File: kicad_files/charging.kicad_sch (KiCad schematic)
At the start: 22 parts, among them Q1 AO3400A, Q2 AO3400A, Q3 AO3401A, Q5 Q_PMOS, U2 BQ24172RGYR, U3 CYPD3177-24LQ

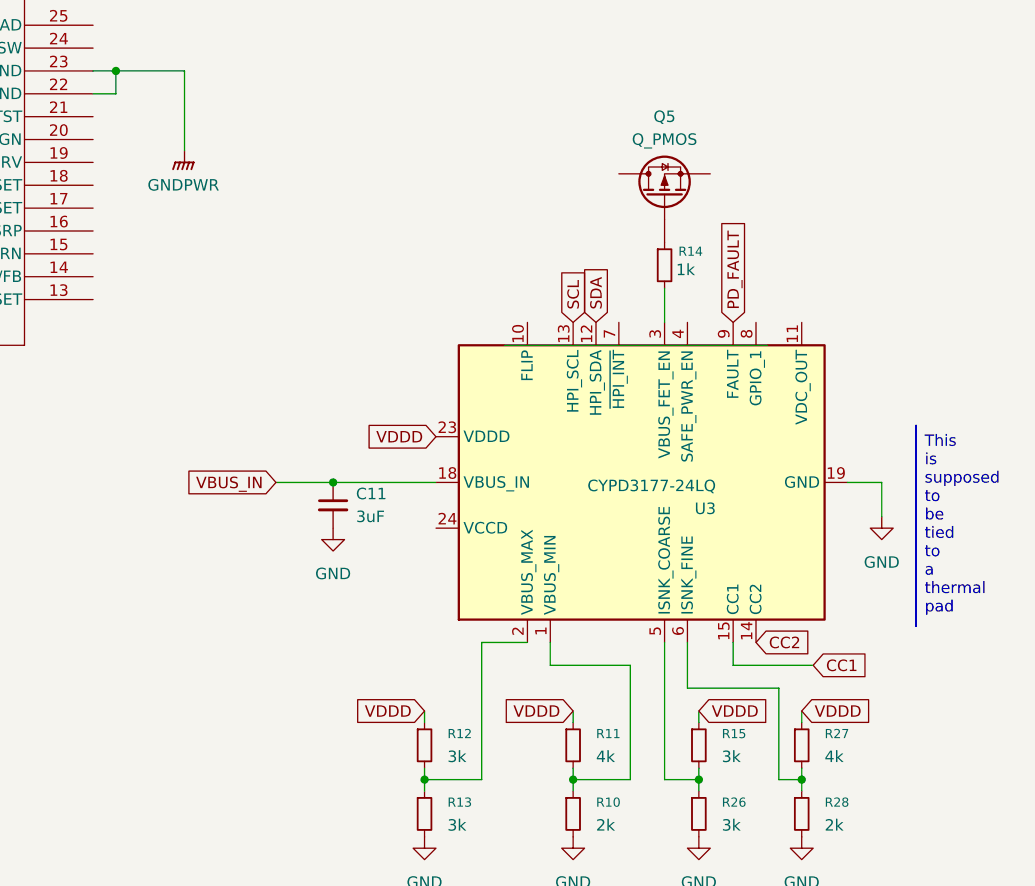
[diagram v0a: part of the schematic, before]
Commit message: fixing up some labels
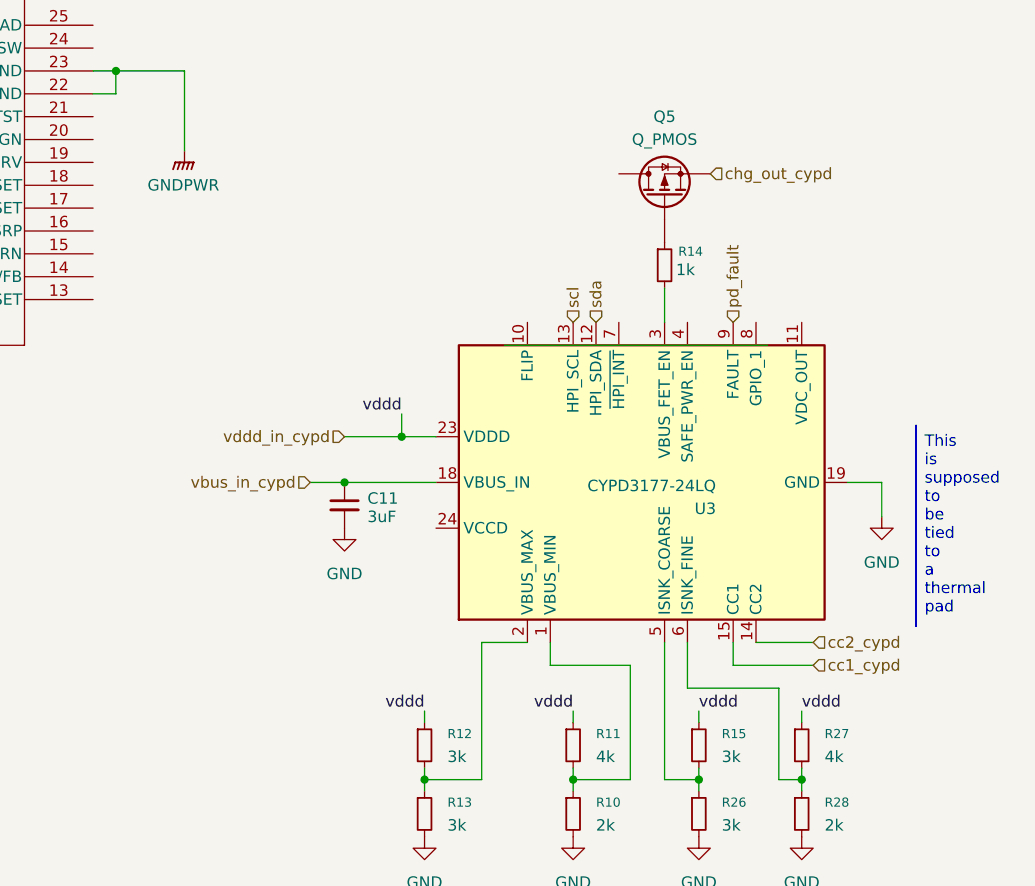
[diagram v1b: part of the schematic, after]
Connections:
- net chg_out_cypd: now reaches Q5.S
- net CC1 renamed cc1_cypd
- net CC2 renamed cc2_cypd
- net PD_FAULT renamed pd_fault
- net SCL renamed scl
- net SDA renamed sda
- net VBUS_IN renamed vbus_in_cypd
- net VDDD renamed vddd_in_cypd
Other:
- moved on the sheet: C11

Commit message: Fix grid alignment issues with charging hierarchical sheet
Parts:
- renumbered R12 to R10, R13 to R11, R11 to R12, R10 to R13, R26 to R20, R27 to R21, R28 to R26

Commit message: A little more progress on BQ24172 IC
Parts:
- added R27: 10m, symbol Device:R_Small
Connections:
- net GNDA: now also C10.1; no longer C10.2
- net Vsys: now also C10.2, C9.2, U2.5 (ACN), R27.2; no longer Q2.3 (D)
- net at C9.1: now also Q2.3 (D), U2.6 (ACP), R27.1; no longer U2.5 (ACN)
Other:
- moved on the sheet: C10, C9, Q1, Q2, Q3, R9

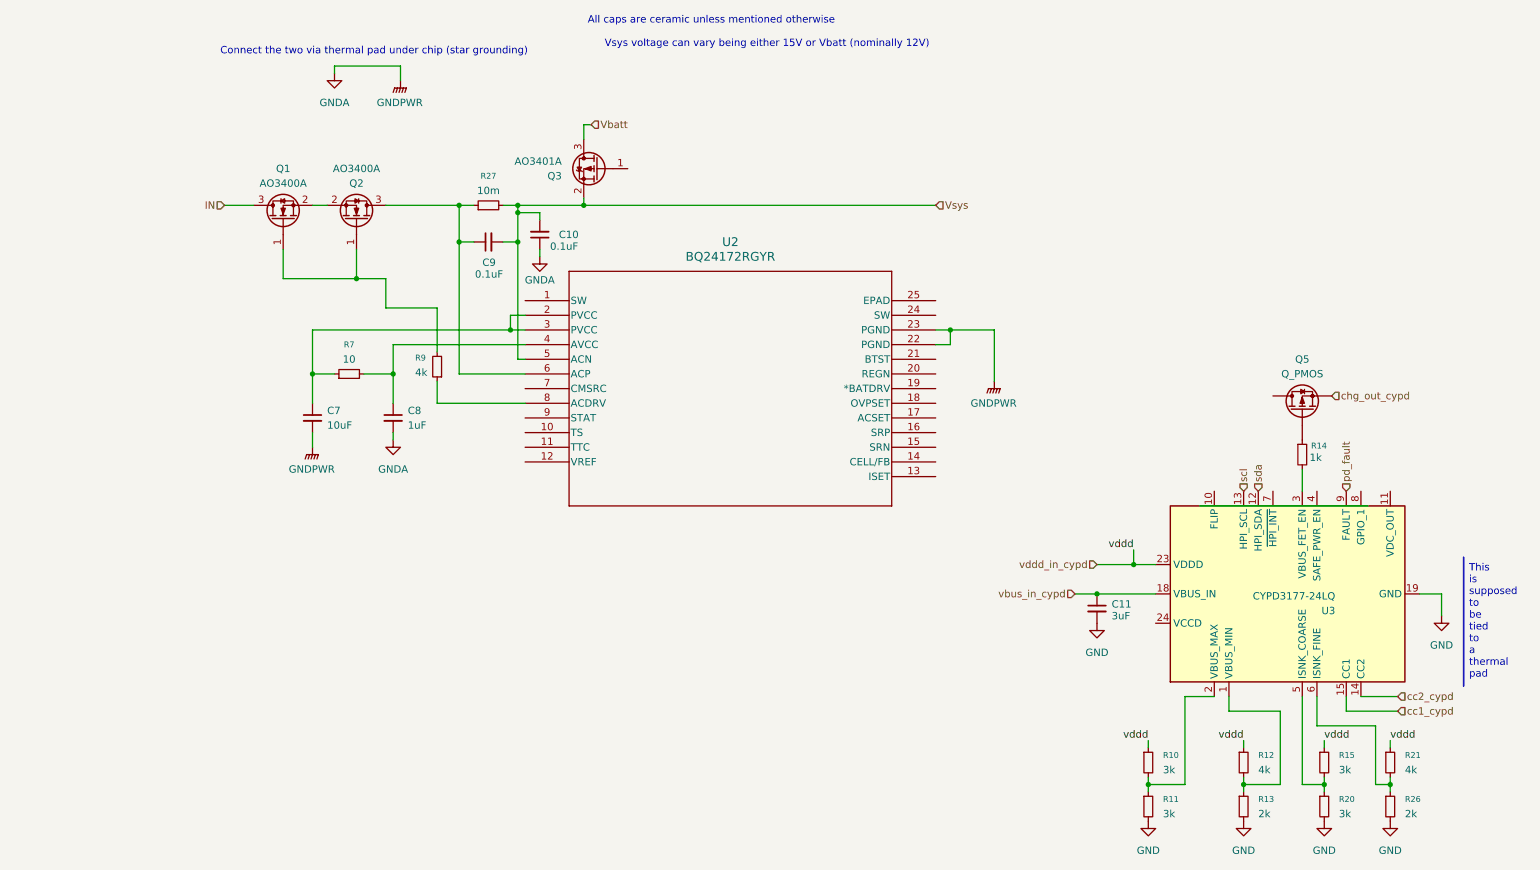
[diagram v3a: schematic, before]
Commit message: More progress on the wiring the BQ24172
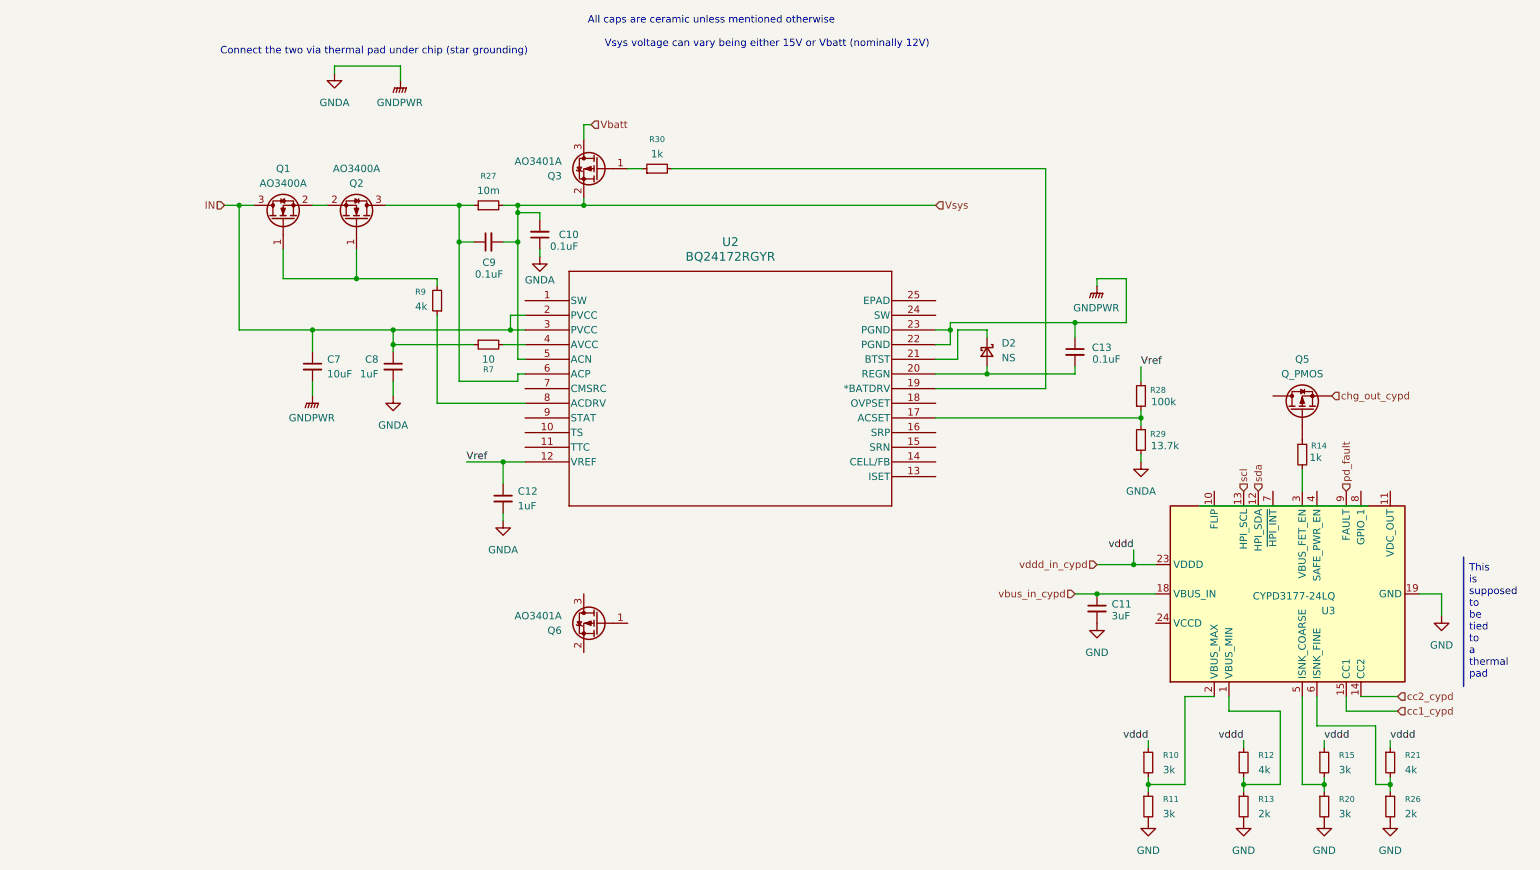
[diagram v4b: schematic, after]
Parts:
- added C12: 1uF, symbol Device:C_Small
- added C13: 0.1uF, symbol Device:C_Small
- added D2: NS, symbol Device:D_Schottky_Small
- added Q6: AO3401A, Package_TO_SOT_SMD:SOT-23, symbol Transistor_FET:AO3401A
- added R28: 100k, symbol Device:R_Small
- added R29: 13.7k, symbol Device:R_Small
- added R30: 1k, symbol Device:R_Small
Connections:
- net GNDA: now also C12.2, C13.1, R29.1
- net IN: now also C7.1, C8.1, R7.1, U2.2 (PVCC), U2.3 (PVCC)
- net at R7.2, U2.4 (AVCC): no longer C8.1
- net at Q3.1 (G): now also R30.1
- net Vref: now reaches U2.12 (VREF)
- net Vref: now also C12.1, R28.2
- net at U2.17 (ACSET): now also R28.1, R29.2
- net at U2.19 (*BATDRV): now also R30.2
- net at U2.20 (REGN): now also C13.2, D2.2 (A)
- net at U2.21 (BTST): now also D2.1 (K)
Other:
- moved on the sheet: C7, C8, R7, R9

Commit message: Start implementation of magetics in converter stage of charger
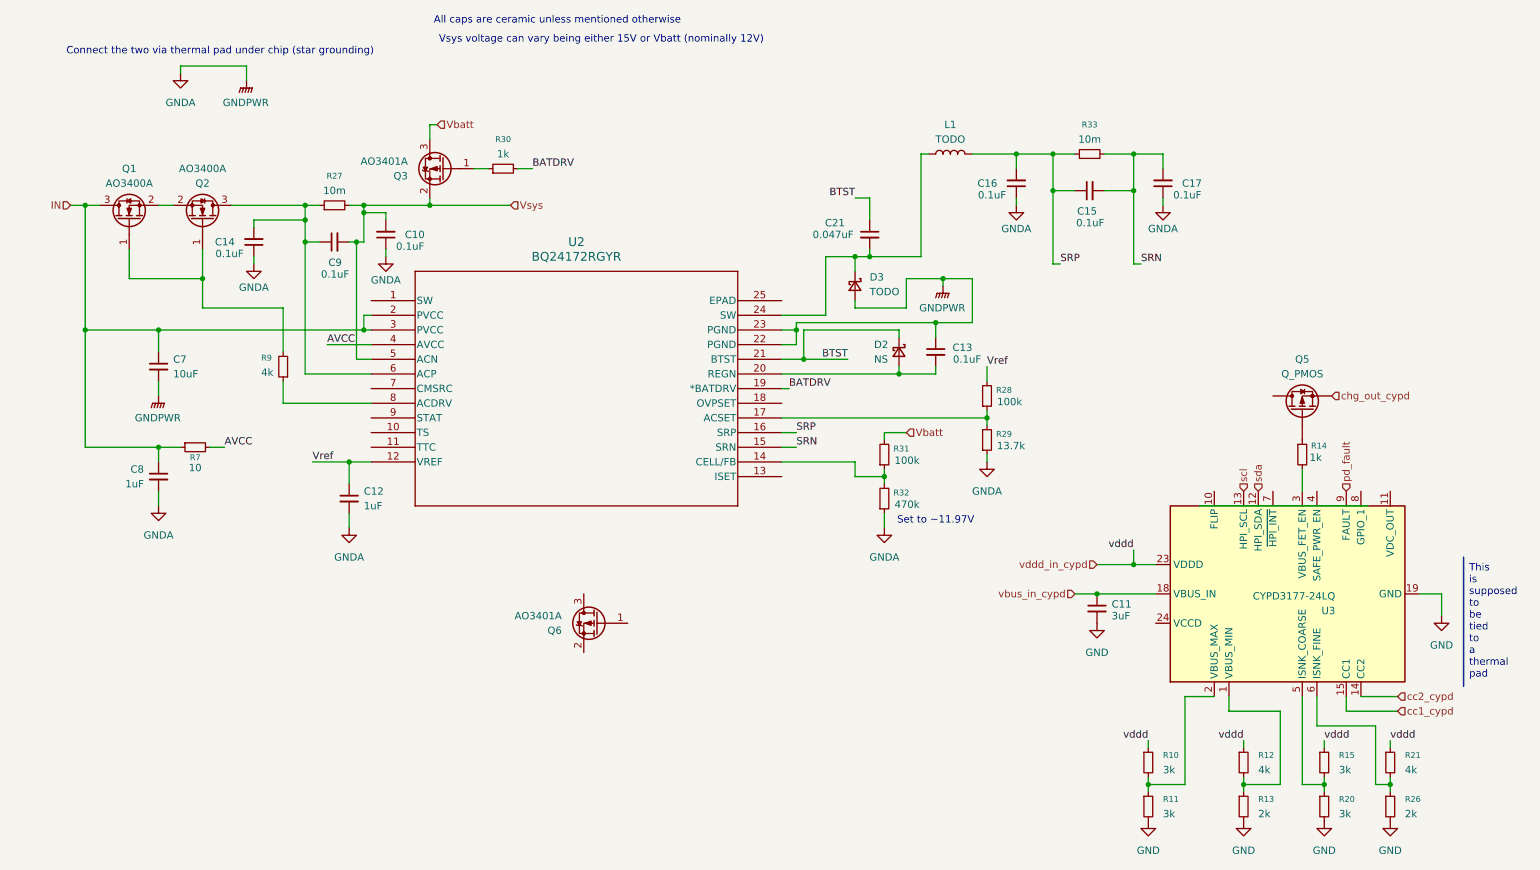
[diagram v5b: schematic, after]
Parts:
- added C14, C15, C16, C17: 0.1uF, symbol Device:C_Small
- added C21: 0.047uF, symbol Device:C_Small
- added D3: TODO, symbol Device:D_Schottky_Small
- added L1: TODO, symbol Device:L
- added R31: 100k, symbol Device:R_Small
- added R32: 470k, symbol Device:R_Small
- added R33: 10m, symbol Device:R_Small
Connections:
- net GNDA: now also C14.1, C16.1, C17.1, D3.2 (A), R32.1
- net Vbatt: now also R31.2
- net at C9.1, Q2.3 (D), R27.1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: now also C14.2
- net AVCC: now reaches R7.2, U2.4 (AVCC)
- net at U2.14 (CELL/FB): now also R31.1, R32.2
- net SRN: now reaches U2.15 (SRN)
- net SRN: now also C15.2, C17.2, R33.2
- net SRP: now reaches U2.16 (SRP)
- net SRP: now also C15.1, C16.2, L1.2, R33.1
- net BATDRV: now reaches R30.2, U2.19 (*BATDRV)
- net BTST: now reaches D2.1 (K), U2.21 (BTST)
- net BTST: now also C21.1
- net at U2.24 (SW): now also C21.2, D3.1 (K), L1.1
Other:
- note added: "Set to ~11.97V"
- moved on the sheet: C10, C12, C13, C7, C8, C9, D2, Q1, Q2, Q3, R27, R28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
